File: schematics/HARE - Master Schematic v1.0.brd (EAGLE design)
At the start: 105.1 x 80 mm, 93 parts, among them IC1 NE5532N, IC2 NE5532N, IC3 FT232RL, IC4 NE5532N, IC5 7805DT, IC6 AT25P, J1 9V, J2 STEREOSW, J3 STEREOSW, Q1 16 MHz, SW1 3PDT, SW2 Reset Button, U1 ATMEGA328P-PU, U2 MCP4921-E/P, X2 USB-B-H

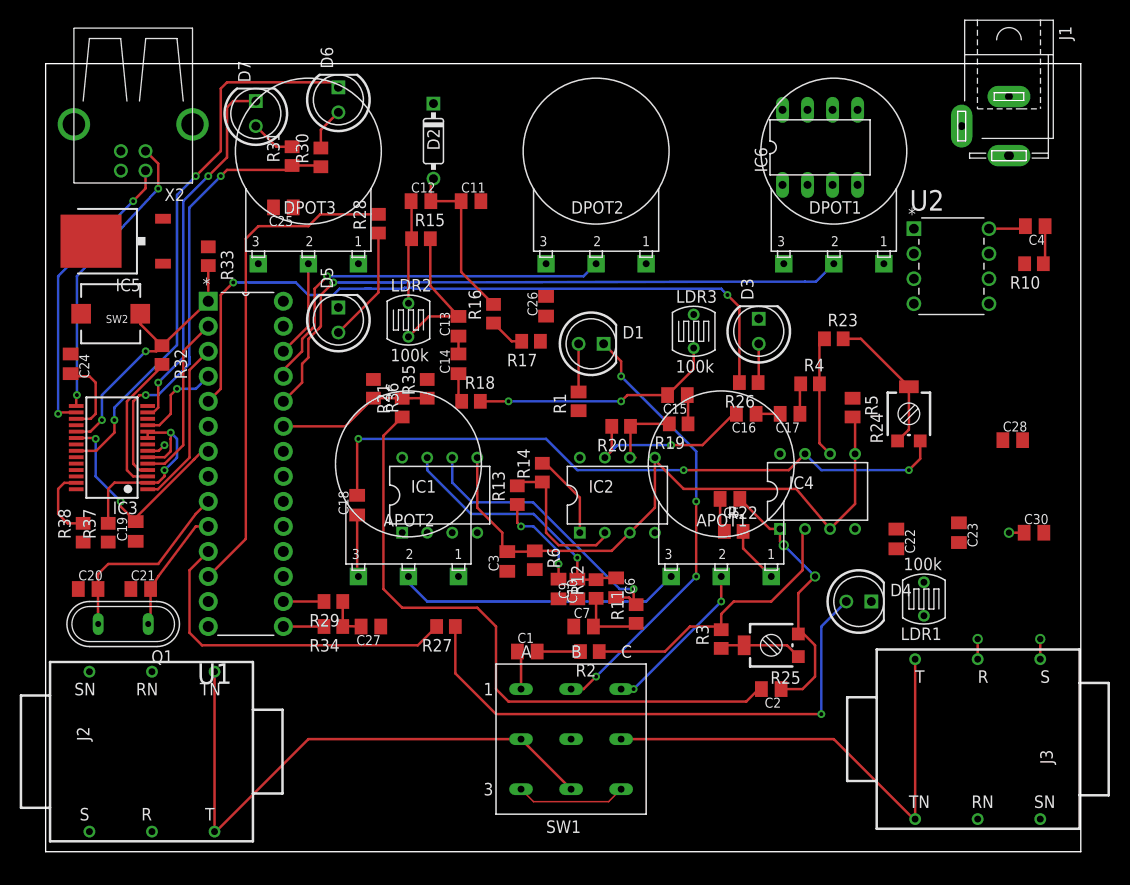
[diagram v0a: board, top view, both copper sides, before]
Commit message: The beginning of a board.  Need to route power and move some resistors and capacitors
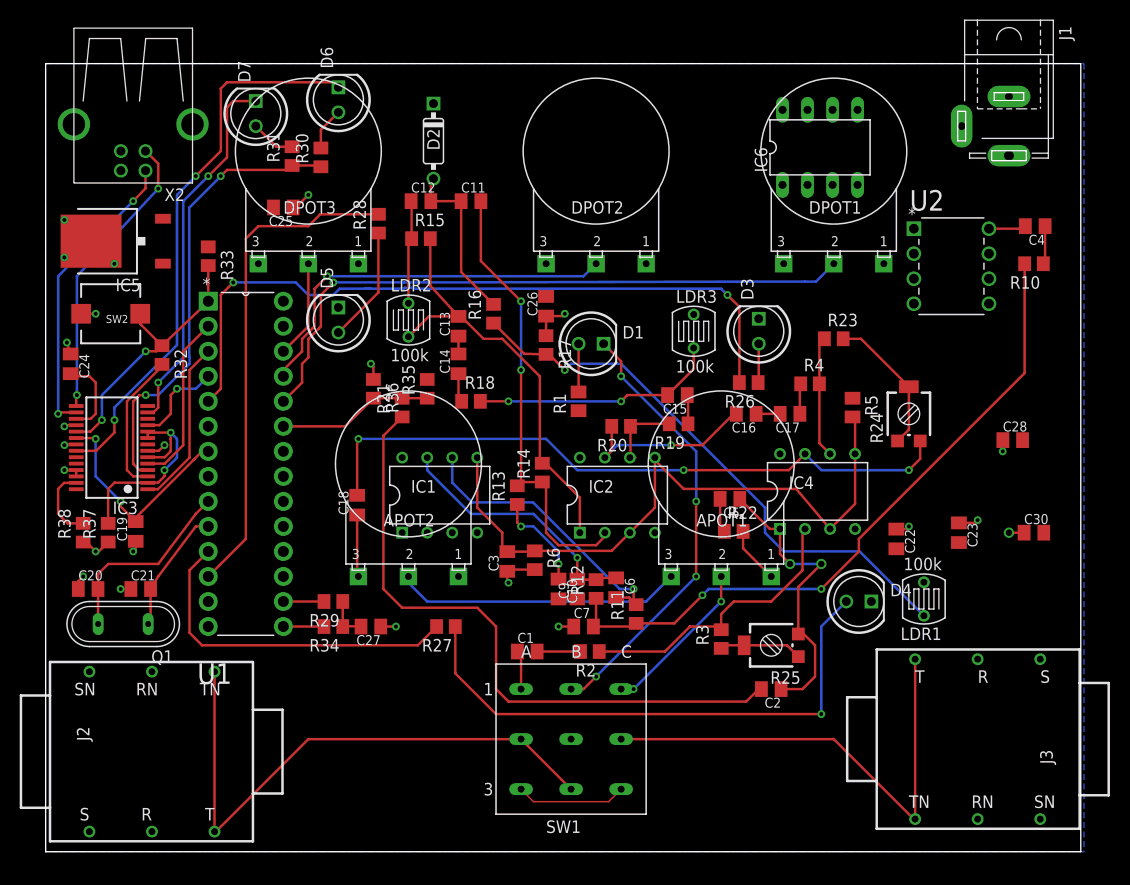
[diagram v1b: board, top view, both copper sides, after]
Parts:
- moved R17 1.57 mm to (50.8, 51.4), turned to 270 degrees
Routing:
- net N$16: track 7.44 -> 69.2 mm, vias 0 -> 2
- net N$29: track 3.62 -> 58.0 mm, vias 0 -> 1
- net GND: track 7.58 -> 46.7 mm, vias 4 -> 23
- net N$22: track 15.2 -> 45.8 mm, vias 0 -> 2
- net N$23: track 23.3 -> 43.1 mm
- net N$37: track 27.5 -> 29.9 mm
- added copper zone on layer 16, net GND

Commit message: First pass at board layout and updated schematic
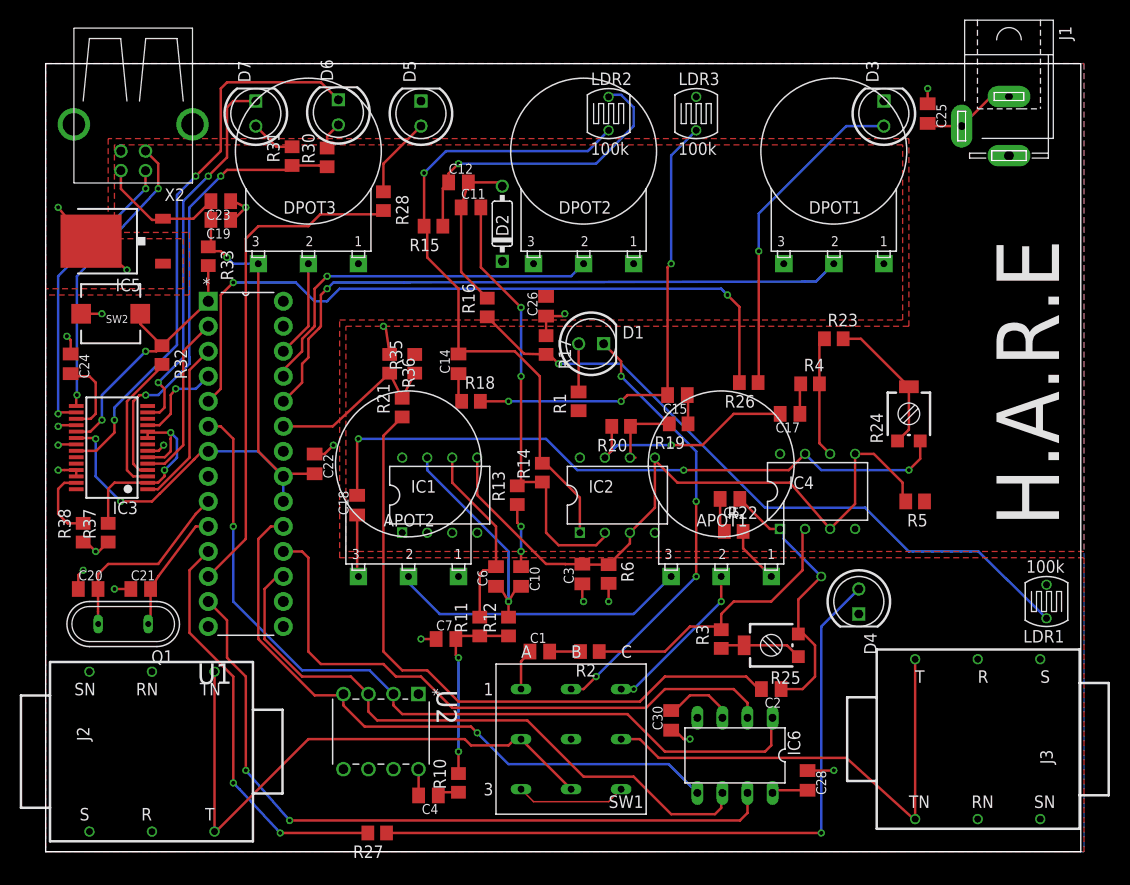
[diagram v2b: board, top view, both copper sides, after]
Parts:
- removed C13, C16, C9: 1uF, resistor:C0805K
- removed C27: 4.7nF, resistor:C0805K
- removed R29: 1MEG, resistor:R0805
- removed R34: 3.9k, resistor:R0805
- moved C4 84.5 mm to (38.9, 5.71)
- moved C23 82.1 mm to (17.8, 66.0), turned to 180 degrees
- moved U2 80.8 mm to (30.2, 8.38), turned to 270 degrees
- moved R10 78.7 mm to (41.9, 6.99), turned to 90 degrees
- moved C25 66.1 mm to (89.5, 74.9), turned to 270 degrees
- moved IC6 62.3 mm to (70.0, 9.78), turned to 180 degrees
- moved C22 59.5 mm to (27.3, 39.4)
- moved C30 41.5 mm to (63.5, 13.3), turned to 90 degrees
- moved C28 40.3 mm to (77.3, 7.24), turned to 270 degrees
- moved C19 32.8 mm to (17.8, 64.1), turned to 180 degrees
- moved LDR2 29.2 mm to (57.1, 74.9)
- moved D3 25.5 mm to (85.1, 74.9)
- moved D5 22.6 mm to (38.1, 74.9)
- moved LDR3 22.1 mm to (66.0, 74.9)
- moved R27 22.1 mm to (33.7, 1.91)
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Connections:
- removed net DAC_OUT: C27.2, R29.1, R34.1
- removed net N$18: C6.1, C9.2, IC1.7, R12.2
- removed net N$23: C13.2, IC2.1, LDR2.2, R14.2, R15.2
- removed net N$34: C16.2, IC2.7, R20.2
- removed net N$50: R29.2, U1.16
- removed net N$55: R34.2, U1.15
- net EXT_MEM_CS: now also U1.6, U2.2
- net EXT_MEM_HOLD: now also U1.13
- net EXT_MEM_MISO: now also U1.18
- net EXT_MEM_MOSI: now also U1.19, U2.4
- net EXT_MEM_SCK: now also U1.17, U2.3
- net GND: no longer C27.1
- net VCA_IN: now also IC2.1, LDR2.2, R14.2, R15.2; no longer C13.1
- net VCA_OUT: now also IC2.7, R20.2; no longer C16.1
- net VCF_IN: now also C6.1, IC1.7, R12.2; no longer C9.1
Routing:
- net EXT_MEM_CS: track 0.00 -> 84.3 mm, vias 0 -> 1
- net EXT_MEM_HOLD: track 0.00 -> 74.3 mm, vias 0 -> 2
- net 5V: track 22.6 -> 92.2 mm, vias 2 -> 3
- net VCA_IN: track 1.81 -> 67.5 mm, vias 0 -> 1
- net EXT_MEM_MOSI: track 0.00 -> 65.0 mm, vias 0 -> 1
- net EXT_MEM_SCK: track 0.00 -> 64.1 mm
- net EXT_MEM_MISO: track 0.00 -> 62.2 mm
- net N$16: track 69.2 -> 19.2 mm
- net N$23: track 43.1 -> 0.00 mm
- net N$61: track 3.96 -> 33.6 mm, vias 0 -> 1
- net N$18: track 26.4 -> 0.00 mm, vias 1 -> 0
- net N$31: track 25.1 -> 47.3 mm, vias 2 -> 3
- net VCF_IN: track 1.91 -> 23.9 mm, vias 0 -> 1
- net N$25: track 10.5 -> 31.4 mm, vias 0 -> 1
- net VCA_OUT: track 2.44 -> 23.1 mm, vias 0 -> 1
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- added copper zone on layer 1, net 5V
- added copper zone on layer 1, net VCC
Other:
- board text added: "H.A.R.E"

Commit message: ZACK DEFINITELY DID ITgit add schematics/HARE\ -\ Master\ Schematic\ v1.0.sch schematics/HARE\ -\ Master\ Schematic\ v1.0.brd !
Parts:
- removed C30: 10uF, resistor:C0805K
- added C13, C9: .1uF, resistor:C0805K
- added C16, C27: 0.1uF, resistor:C0805K
- added C29: 1uF, resistor:C0805K
- added C8: 100nF, resistor:C0805K
- added R29: 10k, resistor:R0805
- added R7, R8, R9: 10k, rcl:M0805
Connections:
- net EXT_MEM_MISO renamed SPI_MISO
- net EXT_MEM_MOSI renamed SPI_MOSI
- net EXT_MEM_SCK renamed SPI_SCK
- removed net 5V: C19.2, C22.2, C23.2, C26.2, C28.2, C30.2, DPOT1.3, DPOT2.3, DPOT3.3, IC3.20, IC5.2, IC6.3, IC6.8, LDR1.2, R33.1, U1.20, U1.21, U1.7, U2.1, U2.6, X2.VBUS
- removed net EXT_MEM_CS: IC6.1, U1.6, U2.2
- removed net EXT_MEM_HOLD: IC6.7, U1.13
- new net +5V: C19.2, C22.2, C23.2, C26.2, C27.1, C28.2, C8.2, DPOT1.3, DPOT2.3, DPOT3.3, IC3.20, IC5.2, IC6.8, LDR1.2, R29.2, R33.1, R7.1, R8.1, R9.1, U1.20, U1.21, U1.7, U2.1, U2.6, X2.VBUS
- new net DAC_CS: IC6.7, R7.2, U1.13
- new net MEM_CS: IC6.1, R29.1, R9.2, U1.6, U2.2
- new net N$18: IC6.3, R8.2
- net GND: now also C13.2, C16.2, C27.2, C29.1, C8.1, C9.1; no longer C30.1
- net VCC: now also C13.1, C16.1, C29.2, C9.2
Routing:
- net 5V: track 92.2 -> 0.00 mm, vias 3 -> 0
- net +5V: track 0.00 -> 84.8 mm, vias 0 -> 3
- net MEM_CS: track 0.00 -> 84.3 mm, vias 0 -> 1
- net EXT_MEM_CS: track 84.3 -> 0.00 mm, vias 1 -> 0
- net EXT_MEM_HOLD: track 74.3 -> 0.00 mm, vias 2 -> 0
- net DAC_CS: track 0.00 -> 74.3 mm, vias 0 -> 2
- net N$18: track 0.00 -> 6.95 mm
- net GND: track 53.7 -> 51.4 mm, vias 21 -> 20
- net SPI_SCK: track 64.1 -> 63.5 mm
- added copper zone on layer 1, net +5V
- removed copper zone on layer 1, net 5V

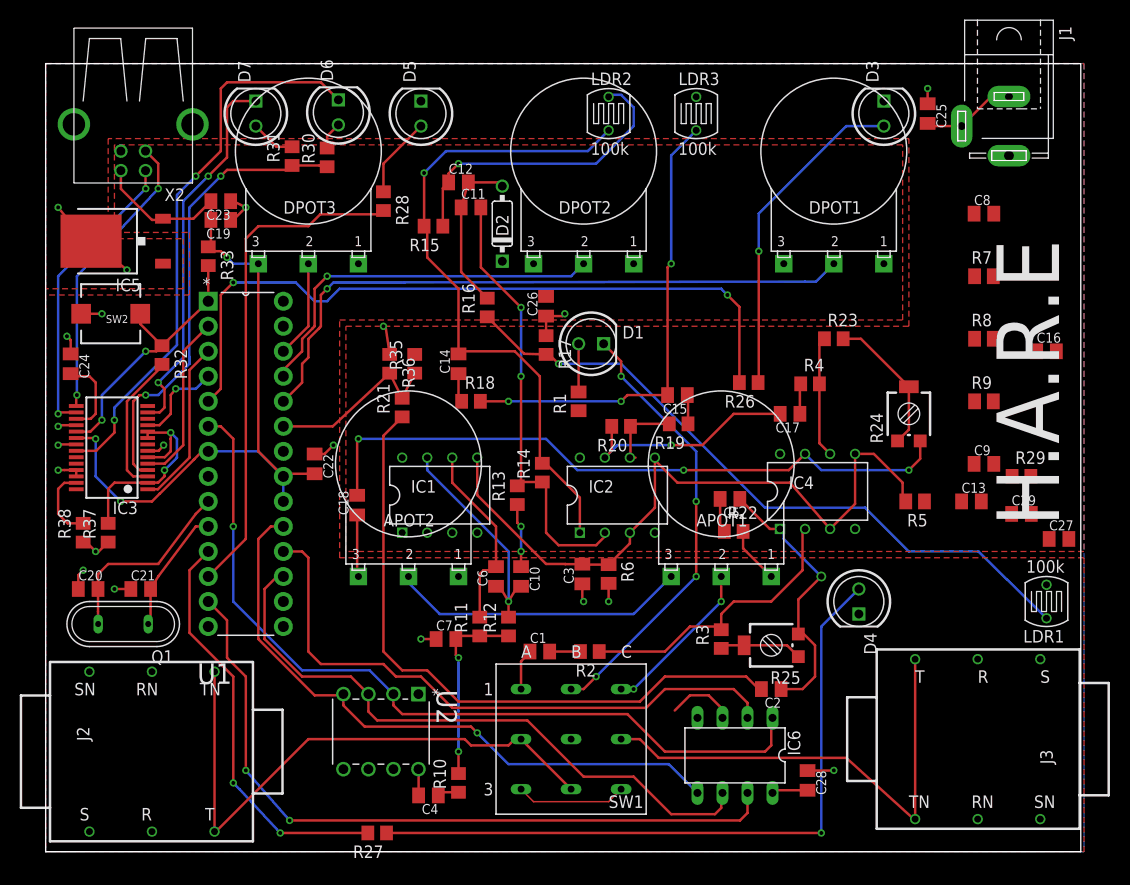
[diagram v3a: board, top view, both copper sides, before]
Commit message: Adding initial routing for footswitch cutout
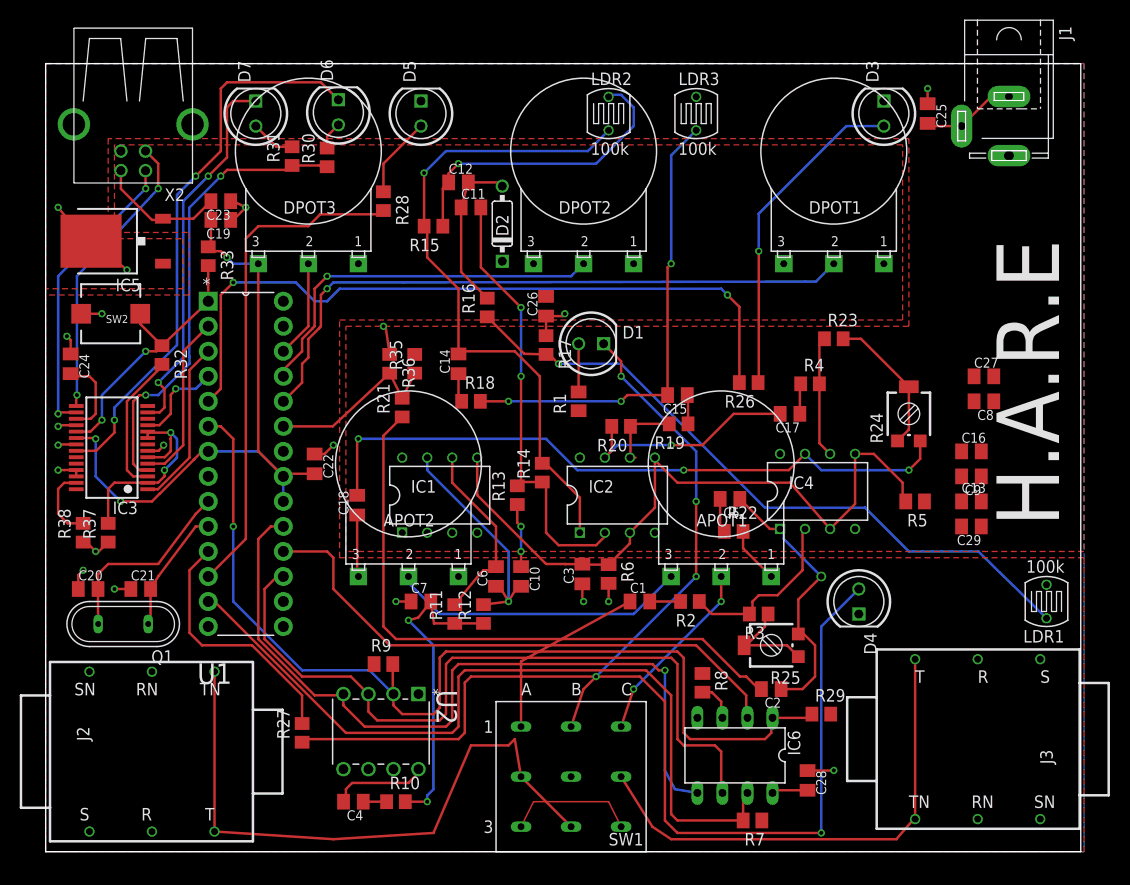
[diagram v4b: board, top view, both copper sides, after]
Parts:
- moved R9 66.5 mm to (34.3, 19.1)
- moved R7 60.0 mm to (71.8, 3.17), turned to 180 degrees
- moved R8 45.1 mm to (66.7, 17.1), turned to 270 degrees
- moved R29 31.5 mm to (78.7, 14.0)
- moved C8 19.0 mm to (95.2, 45.7), turned to 180 degrees
- moved C27 18.2 mm to (95.2, 48.3)
- moved R27 12.7 mm to (26.0, 12.1), turned to 90 degrees
- moved C16 12.7 mm to (94.0, 40.6)
- moved C1 11.4 mm to (60.3, 25.4)
- moved R2 11.4 mm to (65.4, 25.4)
- moved C4 7.65 mm to (31.2, 5.08)
- moved R10 6.63 mm to (35.6, 5.08), turned to 0 degrees
- moved C29 5.24 mm to (94.0, 33.0), turned to 180 degrees
- moved R3 4.58 mm to (72.4, 24.1), turned to 180 degrees
- moved C7 4.58 mm to (38.1, 25.4)
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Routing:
- net N$59: track 70.5 -> 98.4 mm
- net MEM_CS: track 84.3 -> 102.7 mm
- net N$58: track 42.0 -> 26.0 mm, vias 2 -> 0
- net N$9: track 4.16 -> 19.2 mm
- net SPI_MOSI: track 65.0 -> 79.5 mm
- net N$16: track 19.2 -> 32.3 mm
- net SPI_SCK: track 63.5 -> 76.2 mm
- net N$11: track 29.5 -> 18.0 mm
- net DAC_CS: track 74.3 -> 81.8 mm, vias 2 -> 0
- net N$12: track 2.67 -> 9.82 mm
- net INPUT: track 58.9 -> 63.9 mm
- net SPI_MISO: track 62.2 -> 57.2 mm
- net N$36: track 66.7 -> 63.1 mm
- net N$18: track 6.95 -> 4.00 mm
- net N$8: track 44.9 -> 47.7 mm
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
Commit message: Updated the board file to include cutout for foot switch and some greenburg recommendations
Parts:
- removed SW1: 3PDT, gm-switches:3PDT
- added SV1: FtSW1, con-lstb:MA03-1
- added SV2: FtSW2, con-lstb:MA03-1
- moved C9 97.4 mm to (1.27, 67.9), turned to 270 degrees
- moved C8 94.1 mm to (1.27, 40.9), turned to 90 degrees
- moved C27 64.7 mm to (37.5, 19.1), turned to 90 degrees
- moved C16 55.9 mm to (38.1, 41.9)
- moved C13 41.1 mm to (53.3, 41.9), turned to 180 degrees
- moved C29 23.9 mm to (71.8, 41.9), turned to 0 degrees
- moved R10 6.35 mm to (29.2, 5.08), turned to 180 degrees
- moved C4 4.19 mm to (35.4, 5.08), turned to 0 degrees
- moved C2 1.91 mm to (75.6, 16.5)
- moved IC6 1.91 mm to (71.9, 9.78)
- moved R25 1.91 mm to (75.6, 21.0)
- moved R7 1.91 mm to (73.7, 3.17)
- moved R8 1.91 mm to (68.6, 17.1)
- moved C28 1.27 mm to (78.6, 7.24)
- moved R9 1.27 mm to (33.0, 19.1)
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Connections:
- removed net BYPASS: SW1.A3, SW1.C3
- removed net N$15: APOT1.2, SW1.C1
- removed net N$19: J3.T, J3.TN, SW1.C2
- removed net N$9: C1.1, SW1.A1
- new net A_IN: C1.1, SV1.2
- new net A_OUT: APOT1.2, SV2.3
- new net OUTPUT: J3.T, J3.TN, SV2.2
- new net PWR_LED: D1.K, SV1.3
- net DAC_CS: now also R29.1, U2.2; no longer IC6.7, R7.2
- net GND: now also SV2.1; no longer SW1.B2
- net INPUT: now also SV1.1; no longer SW1.A2, SW1.B3
- net MEM_CS: no longer R29.1, U2.2
- net N$8: now also IC6.7, R7.2; no longer D1.K, SW1.B1
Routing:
- net PWR_LED: track 0.00 -> 66.3 mm, vias 0 -> 1
- net N$19: track 50.2 -> 0.00 mm
- net N$8: track 47.7 -> 0.00 mm, vias 4 -> 0
- net OUTPUT: track 0.00 -> 43.1 mm
- net A_IN: track 0.00 -> 36.4 mm, vias 0 -> 1
- net INPUT: track 63.9 -> 40.3 mm
- net A_OUT: track 0.00 -> 23.2 mm, vias 0 -> 1
- net N$9: track 19.2 -> 0.00 mm
- net N$15: track 19.1 -> 0.00 mm, vias 2 -> 0
- net BYPASS: track 13.3 -> 0.00 mm
- net GND: track 51.4 -> 63.9 mm, vias 20 -> 25
- net DAC_CS: track 81.8 -> 75.2 mm
- net N$16: track 32.3 -> 38.8 mm
- net N$12: track 9.82 -> 3.62 mm
- net +5V: track 84.8 -> 89.4 mm
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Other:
- outline, holes or cut-outs redrawn
- board text added: "PSU Team 13"
- board text added: "Rev 1.0"
